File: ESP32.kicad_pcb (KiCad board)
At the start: 2 copper layers, 48 x 37 mm, 29 parts, among them J1 USB_B_Micro, J2 BATT, J3 PMS7003 Connector, J5 UART, Q1 AO3401A, SW1 RESET, SW2 BOOTSEL, U1 ESP32-C3-MINI-1, U2 AMS1117-3.3, U3 AMS1117-5.0

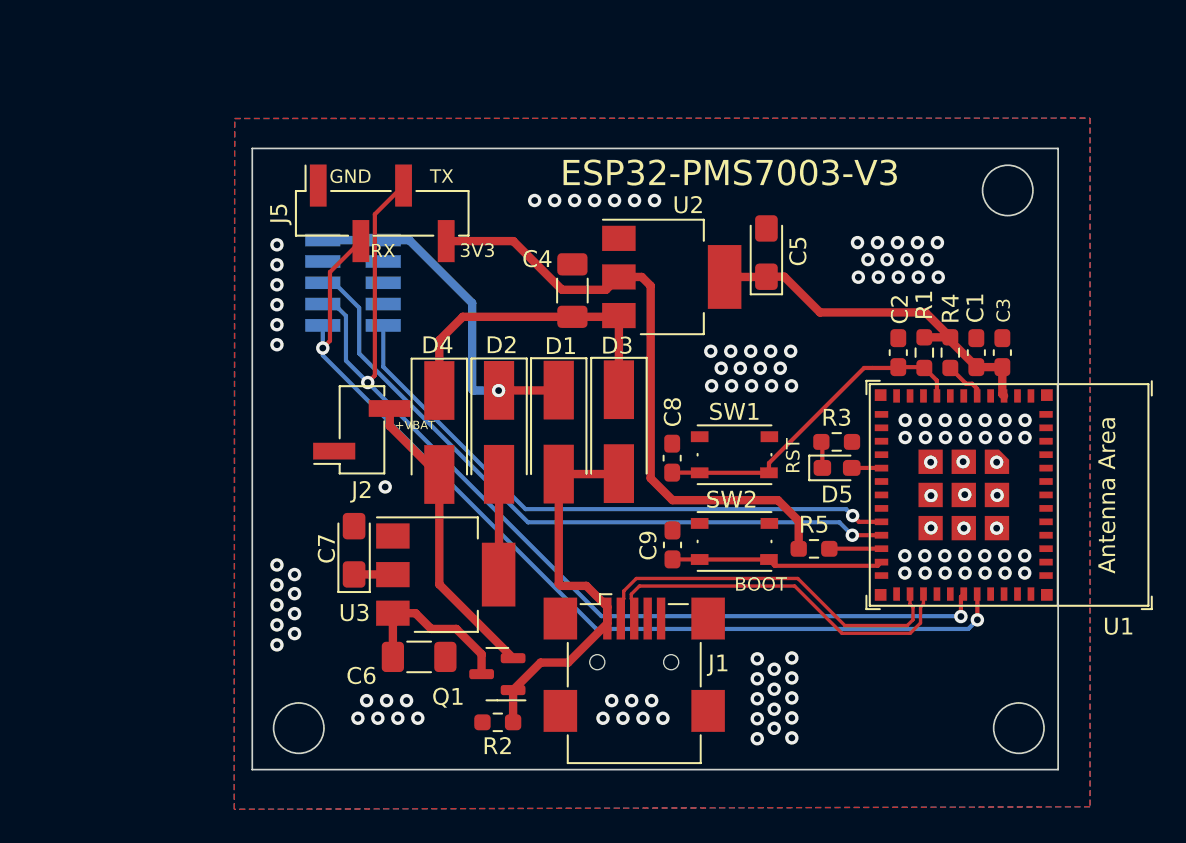
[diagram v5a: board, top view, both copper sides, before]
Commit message: Replaced linear regulators with buck converters
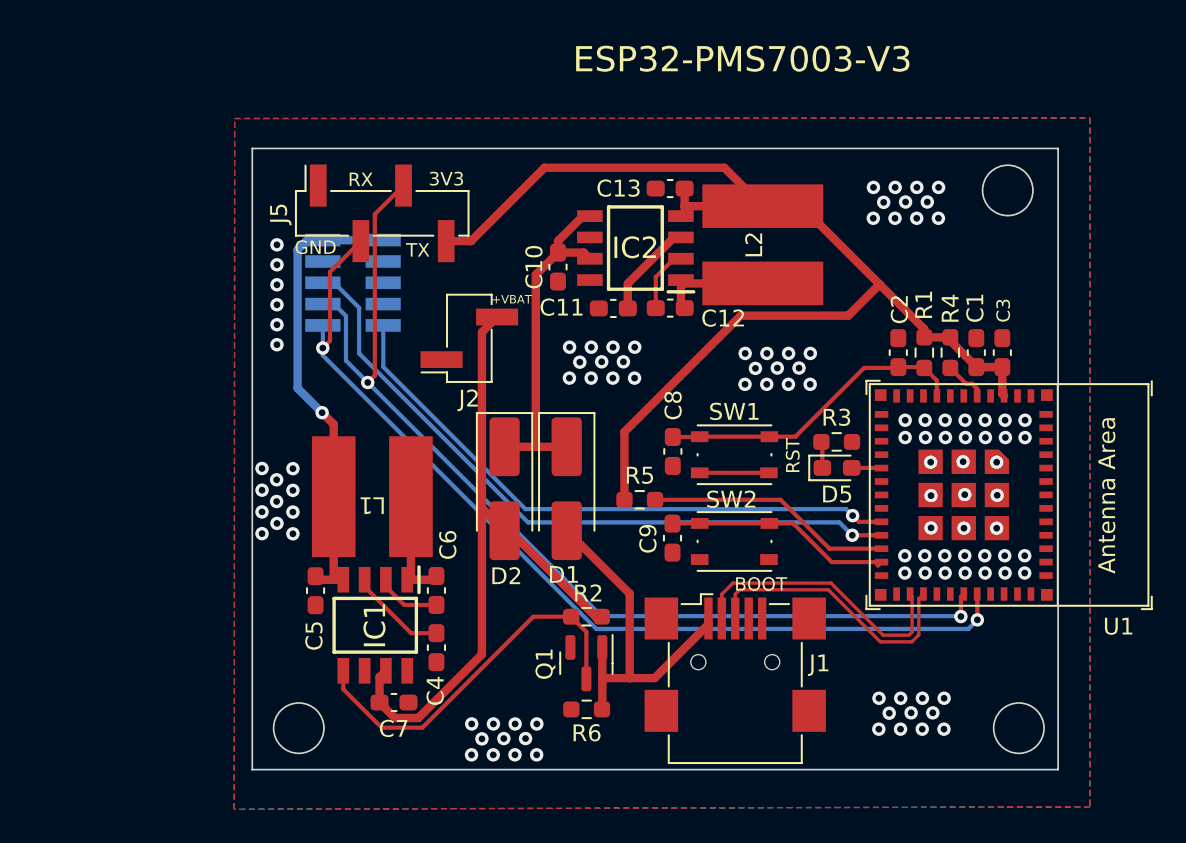
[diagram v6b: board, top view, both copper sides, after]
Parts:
- removed D3, D4: SS14, Diode_SMD:D_SMA_Handsoldering
- removed U2: AMS1117-3.3, Package_TO_SOT_SMD:SOT-223-3_TabPin2
- removed U3: AMS1117-5.0, Package_TO_SOT_SMD:SOT-223-3_TabPin2
- added C10: 10u, Capacitor_SMD:C_0603_1608Metric_Pad1.08x0.95mm_HandSolder, F.Cu at (108.2, 67.1)
- added C11: 1u, Capacitor_SMD:C_0603_1608Metric_Pad1.08x0.95mm_HandSolder, F.Cu at (111.5, 69.5)
- added C12: 100n, Capacitor_SMD:C_0603_1608Metric_Pad1.08x0.95mm_HandSolder, F.Cu at (114.9, 69.5)
- added C13: 22u, Capacitor_SMD:C_0603_1608Metric_Pad1.08x0.95mm_HandSolder, F.Cu at (114.9, 62.4)
- added IC1: L6981C50DR, DC Converters:SOIC127P600X175-8N, F.Cu at (97.3, 88.4)
- added IC2: L6981C33DR, DC Converters:SOIC127P600X175-8N, F.Cu at (112.8, 65.9)
- added L1: 33u, Inductor_SMD:L_Murata_29xxxC, F.Cu at (97.2, 80.7)
- added L2: 33u, Inductor_SMD:L_Murata_29xxxC, F.Cu at (120.4, 65.7)
- added R6: 10k, Resistor_SMD:R_0603_1608Metric_Pad0.98x0.95mm_HandSolder, F.Cu at (109.9, 93.4)
- C4: value 10u -> 1u; footprint Capacitor_SMD:C_1206_3216Metric_Pad1.33x1.80mm_HandSolder -> Capacitor_SMD:C_0603_1608Metric_Pad1.08x0.95mm_HandSolder
- C5: value 10u -> 22u; footprint Capacitor_Tantalum_SMD:CP_EIA-3216-18_Kemet-A_Pad1.58x1.35mm_HandSolder -> Capacitor_SMD:C_0603_1608Metric_Pad1.08x0.95mm_HandSolder
- C6: value 10u -> 100n; footprint Capacitor_SMD:C_1206_3216Metric_Pad1.33x1.80mm_HandSolder -> Capacitor_SMD:C_0603_1608Metric_Pad1.08x0.95mm_HandSolder
- C7: footprint Capacitor_Tantalum_SMD:CP_EIA-3216-18_Kemet-A_Pad1.58x1.35mm_HandSolder -> Capacitor_SMD:C_0603_1608Metric_Pad1.08x0.95mm_HandSolder
- Q1: value AO3401A -> AO3400A
- moved C5 33.6 mm to (93.8, 86.3), turned to -90 degrees
- moved C4 22.8 mm to (101.0, 89.7), turned to -90 degrees
- moved R5 10.8 mm to (113.1, 80.9)
- moved C7 9.37 mm to (98.4, 93.0), turned to 0 degrees
- moved J2 8.40 mm to (102.9, 71.3)
- moved R2 8.22 mm to (109.9, 87.9)
- moved J1 6.02 mm to (118.8, 90.6)
- moved Q1 5.34 mm to (109.9, 90.7), turned to -90 degrees
- moved C6 4.09 mm to (101.0, 86.3), turned to 90 degrees
- moved D1 3.41 mm to (108.7, 80.3)
- moved D2 3.38 mm to (105.0, 80.3)
- moved C9 0.41 mm to (115.0, 83.2)
- moved C8 0.40 mm to (115.0, 78.0)
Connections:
- net /USB_D+ renamed USB_D+
- net /USB_D- renamed USB_D-
- C4 pad 1: /3v3RI -> Net-(IC1-VCC)
- C5 pad 1: +3V3 -> +5V
- C6 pad 1: /5vRI -> Net-(IC1-BOOT)
- C6 pad 2: GND -> Net-(IC1-SW)
- C7 pad 1: /5vRO -> +BATT
- C8 pad 1: GND -> EN_DLY
- C8 pad 2: EN_DLY -> GND
- C9 pad 1: GND -> BOOTSEL
- C9 pad 2: BOOTSEL -> GND
- D1 pad 1: +5V -> Net-(D1-K)
- D2 pad 1: +5V -> Net-(D1-K)
- D2 pad 2: /5vRO -> +BATT
- Q1 pad 2: +BATT -> GND
- Q1 pad 3: /5vRI -> Net-(IC1-EN/CLKIN)
- R2 pad 1: VBUS -> +BATT
- R2 pad 2: GND -> Net-(IC1-EN/CLKIN)
- SW1 pad 1: GND -> EN_DLY
- SW1 pad 2: EN_DLY -> GND
- SW2 pad 1: GND -> BOOTSEL
- SW2 pad 2: BOOTSEL -> GND
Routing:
- net +BATT: track 17.9 -> 41.0 mm
- net Net-(IC1-EN/CLKIN): track 0.00 -> 22.4 mm
- net Net-(D1-K): track 0.00 -> 21.1 mm
- net /3v3RI: track 18.7 -> 0.00 mm
- net +3V3: track 59.3 -> 71.5 mm
- net Net-(U1-GPIO8): track 3.11 -> 14.7 mm
- net /5vRI: track 10.1 -> 0.00 mm
- net /5vRO: track 8.30 -> 0.00 mm
- net Net-(IC1-SW): track 0.00 -> 6.87 mm
- net +5V: track 20.8 -> 27.6 mm
- net Net-(IC2-SW): track 0.00 -> 6.72 mm
- net Net-(IC1-VCC): track 0.00 -> 5.84 mm
- net Net-(IC2-VCC): track 0.00 -> 5.78 mm
- net USB_D+: track 22.2 -> 16.5 mm
- net USB_D-: track 22.2 -> 16.7 mm
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
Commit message: Schematic + Layout
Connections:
- C6 pad 1: Net-(IC1-BOOT) -> Net-(IC1-SW)
- C6 pad 2: Net-(IC1-SW) -> Net-(IC1-BOOT)
- J3 pad 7: PMS_TX -> PMS_RX
- J3 pad 9: PMS_RX -> PMS_TX
- L1 pad 1: Net-(IC1-SW) -> Net-(IC1-BOOT)
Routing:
- net PMS_RX: track 56.6 -> 57.9 mm
- net PMS_TX: track 61.3 -> 61.9 mm
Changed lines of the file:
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@@
       (stroke (width 0.1) (type solid)) (layer "F.Fab"))
     (pad "1" smd roundrect (at -0.8625 0 90) (size 1.075 0.95) (layers "F.Cu" "F.Paste" "F.Mask") (roundrect_rratio 0.25)
+      (net 41 "Net-(IC1-SW)") (pintype "passive"))
+    (pad "2" smd roundrect (at 0.8625 0 90) (size 1.075 0.95) (layers "F.Cu" "F.Paste" "F.Mask") (roundrect_rratio 0.25)
       (net 34 "Net-(IC1-BOOT)") (pintype "passive"))
-    (pad "2" smd roundrect (at 0.8625 0 90) (size 1.075 0.95) (layers "F.Cu" "F.Paste" "F.Mask") (roundrect_rratio 0.25)
-      (net 41 "Net-(IC1-SW)") (pintype "passive"))
     (model "${KICAD6_3DMODEL_DIR}/Capacitor_SMD.3dshapes/C_0603_1608Metric.wrl"
       (offset (xyz 0 0 0))
@@
       (stroke (width 0.05) (type default)) (fill none) (layer "F.CrtYd"))
     (pad "1" smd rect (at -2.3 0 180) (size 2.6 7.2) (layers "F.Cu" "F.Paste" "F.Mask")
-      (net 41 "Net-(IC1-SW)") (pinfunction "1") (pintype "passive") (thermal_bridge_angle 45))
+      (net 34 "Net-(IC1-BOOT)") (pinfunction "1") (pintype "passive") (thermal_bridge_angle 45))
     (pad "2" smd rect (at 2.3 0 180) (size 2.6 7.2) (layers "F.Cu" "F.Paste" "F.Mask")
       (net 3 "+5V") (pinfunction "2") (pintype "passive") (thermal_bridge_angle 45))
@@
       (net 7 "unconnected-(J3-Pin_6-Pad6)") (pinfunction "Pin_6") (pintype "passive+no_connect"))
     (pad "7" smd rect locked (at 1.8 -1.27 180) (size 2.1 0.75) (layers "B.Cu" "B.Paste" "B.Mask")
-      (net 30 "PMS_TX") (pinfunction "Pin_7") (pintype "passive"))
+      (net 31 "PMS_RX") (pinfunction "Pin_7") (pintype "passive"))
     (pad "8" smd rect locked (at -1.8 -1.27 180) (size 2.1 0.75) (layers "B.Cu" "B.Paste" "B.Mask")
       (net 8 "unconnected-(J3-Pin_8-Pad8)") (pinfunction "Pin_8") (pintype "passive+no_connect"))
     (pad "9" smd rect locked (at 1.8 -2.54 180) (size 2.1 0.75) (layers "B.Cu" "B.Paste" "B.Mask")
-      (net 31 "PMS_RX") (pinfunction "Pin_9") (pintype "passive"))
+      (net 30 "PMS_TX") (pinfunction "Pin_9") (pintype "passive"))
     (pad "10" smd rect locked (at -1.8 -2.54 180) (size 2.1 0.75) (layers "B.Cu" "B.Paste" "B.Mask")
       (net 32 "PMS_SET") (pinfunction "Pin_10") (pintype "passive"))
@@
   (segment (start 96.3676 69.4926) (end 96.3676 72.2122) (width 0.25) (layer "B.Cu") (net 29))
   (segment (start 132.210387 86.709613) (end 132.38 86.54) (width 0.25) (layer "F.Cu") (net 30))
-  (segment (start 96.8781 73.9419) (end 97.3 73.52) (width 0.25) (layer "F.Cu") (net 30))
-  (segment (start 97.3 73.52) (end 97.3 63.92) (width 0.25) (layer "F.Cu") (net 30))
+  (segment (start 99.01 71.66) (end 96.235 74.435) (width 0.25) (layer "F.Cu") (net 30))
   (segment (start 132.210387 87.881597) (end 132.210387 86.709613) (width 0.25) (layer "F.Cu") (net 30))
-  (segment (start 97.3 63.92) (end 99.01 62.21) (width 0.25) (layer "F.Cu") (net 30))
+  (segment (start 99.01 62.21) (end 99.01 71.66) (width 0.25) (layer "F.Cu") (net 30))
+  (via (at 96.235 74.435) (size 0.8) (drill 0.4) (layers "F.Cu" "B.Cu") (net 30))
   (via (at 132.210387 87.881597) (size 0.8) (drill 0.4) (layers "F.Cu" "B.Cu") (net 30))
-  (via (at 96.8781 73.9419) (size 0.8) (drill 0.4) (layers "F.Cu" "B.Cu") (net 30))
-  (segment (start 95.5802 72.644) (end 95.5802 69.9752) (width 0.25) (layer "B.Cu") (net 30))
-  (segment (start 132.210387 87.881597) (end 132.18739 87.8586) (width 0.25) (layer "B.Cu") (net 30))
-  (segment (start 110.7948 87.8586) (end 95.5802 72.644) (width 0.25) (layer "B.Cu") (net 30))
-  (segment (start 94.875 69.27) (end 94.2 69.27) (width 0.25) (layer "B.Cu") (net 30))
-  (segment (start 132.18739 87.8586) (end 110.7948 87.8586) (width 0.25) (layer "B.Cu") (net 30))
-  (segment (start 95.5802 69.9752) (end 94.875 69.27) (width 0.25) (layer "B.Cu") (net 30))
-  (segment (start 133.19 86.55) (end 133.18 86.54) (width 0.25) (layer "F.Cu") (net 31))
-  (segment (start 133.19 88.08) (end 133.19 86.55) (width 0.25) (layer "F.Cu") (net 31))
-  (segment (start 94.6277 71.4623) (end 94.6277 67.3623) (width 0.25) (layer "F.Cu") (net 31))
-  (segment (start 94.2 71.89) (end 94.6277 71.4623) (width 0.25) (layer "F.Cu") (net 31))
-  (segment (start 94.6277 67.3623) (end 96.47 65.52) (width 0.25) (layer "F.Cu") (net 31))
-  (via (at 133.19 88.08) (size 0.8) (drill 0.4) (layers "F.Cu" "B.Cu") (net 31))
-  (via (at 94.2 71.89) (size 0.8) (drill 0.4) (layers "F.Cu" "B.Cu") (net 31))
-  (segment (start 133.19 88.08) (end 132.6494 88.6206) (width 0.25) (layer "B.Cu") (net 31))
-  (segment (start 94.2 72.3306) (end 94.2 70.54) (width 0.25) (layer "B.Cu") (net 31))
-  (segment (start 110.49 88.6206) (end 94.2 72.3306) (width 0.25) (layer "B.Cu") (net 31))
-  (segment (start 132.6494 88.6206) (end 110.49 88.6206) (width 0.25) (layer "B.Cu") (net 31))
+  (segment (start 131.241984 88.85) (end 132.210387 87.881597) (width 0.25) (layer "B.Cu") (net 30))
+  (segment (start 94.2 70.54) (end 94.2 72.4) (width 0.25) (layer "B.Cu") (net 30))
+  (segment (start 96.235 74.435) (end 110.65 88.85) (width 0.25) (layer "B.Cu") (net 30))
+  (segment (start 110.65 88.85) (end 131.241984 88.85) (width 0.25) (layer "B.Cu") (net 30))
+  (segment (start 94.2 72.4) (end 96.235 74.435) (width 0.25) (layer "B.Cu") (net 30))
+  (segment (start 131.910082 88.606597) (end 132.510692 88.606597) (width 0.25) (layer "F.Cu") (net 31))
+  (segment (start 133.18 87.937289) (end 133.18 86.54) (width 0.25) (layer "F.Cu") (net 31))
+  (segment (start 96.47 71.88) (end 95.66 72.69) (width 0.25) (layer "F.Cu") (net 31))
+  (segment (start 96.47 65.52) (end 96.47 71.88) (width 0.25) (layer "F.Cu") (net 31))
+  (segment (start 131.297178 87.993693) (end 131.910082 88.606597) (width 0.25) (layer "F.Cu") (net 31))
+  (segment (start 132.510692 88.606597) (end 133.18 87.937289) (width 0.25) (layer "F.Cu") (net 31))
+  (segment (start 131.073693 87.993693) (end 131.297178 87.993693) (width 0.25) (layer "F.Cu") (net 31))
+  (via (at 131.073693 87.993693) (size 0.8) (drill 0.4) (layers "F.Cu" "B.Cu") (net 31))
+  (via (at 95.66 72.69) (size 0.8) (drill 0.4) (layers "F.Cu" "B.Cu") (net 31))
+  (segment (start 110.963693 87.993693) (end 95.66 72.69) (width 0.25) (layer "B.Cu") (net 31))
+  (segment (start 131.073693 87.993693) (end 110.963693 87.993693) (width 0.25) (layer "B.Cu") (net 31))
+  (segment (start 95.66 72.69) (end 95.66 69.7) (width 0.25) (layer "B.Cu") (net 31))
+  (segment (start 95.66 69.7) (end 95.23 69.27) (width 0.25) (layer "B.Cu") (net 31))
+  (segment (start 95.23 69.27) (end 94.2 69.27) (width 0.25) (layer "B.Cu") (net 31))
   (segment (start 125.76 81.87) (end 126.13 82.24) (width 0.25) (layer "F.Cu") (net 32))
   (segment (start 126.13 82.24) (end 127.48 82.24) (width 0.25) (layer "F.Cu") (net 32))
   (via (at 125.76 81.87) (size 0.8) (drill 0.4) (layers "F.Cu" "B.Cu") (net 32))
-  (segment (start 97.8 73.008204) (end 97.8 70.54) (width 0.25) (layer "B.Cu") (net 32))
-  (segment (start 106.274996 81.4832) (end 97.8 73.008204) (width 0.25) (layer "B.Cu") (net 32))
   (segment (start 125.76 81.87) (end 125.3732 81.4832) (width 0.25) (layer "B.Cu") (net 32))
-  (segment (start 125.3732 81.4832) (end 106.274996 81.4832) (width 0.25) (layer "B.Cu") (net 32))
+  (segment (start 97.8 72.35) (end 97.8 70.54) (width 0.25) (layer "B.Cu") (net 32))
+  (segment (start 106.9332 81.4832) (end 97.8 72.35) (width 0.25) (layer "B.Cu") (net 32))
+  (segment (start 125.3732 81.4832) (end 106.9332 81.4832) (width 0.25) (layer "B.Cu") (net 32))
   (segment (start 99.4595 88.872) (end 100.97 88.872) (width 0.25) (layer "F.Cu") (net 33))
   (segment (start 96.69 86.1025) (end 99.4595 88.872) (width 0.25) (layer "F.Cu") (net 33))
